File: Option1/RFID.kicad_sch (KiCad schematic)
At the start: 1 part, among them J1801 Conn_01x08_Socket

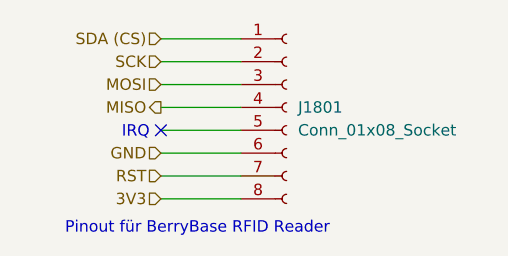
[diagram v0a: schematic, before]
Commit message: Programming Header hinzugefügt für flashen via DevKit
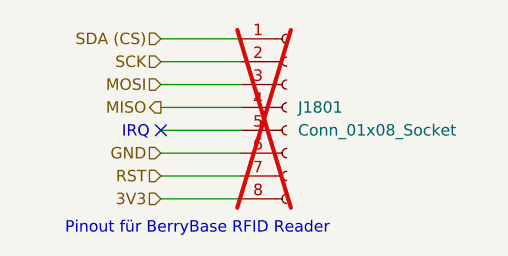
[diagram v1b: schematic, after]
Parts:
- J1801: now not fitted; now left out of the parts list
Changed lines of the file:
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@@
 		(unit 1)
 		(exclude_from_sim no)
-		(in_bom yes)
+		(in_bom no)
 		(on_board yes)
-		(dnp no)
+		(dnp yes)
 		(fields_autoplaced yes)
 		(property "Reference" "J1801"
